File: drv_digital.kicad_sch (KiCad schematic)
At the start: 7 parts, among them U10 74LVC1G19, U11 74HCT595, U12 ULN2803A

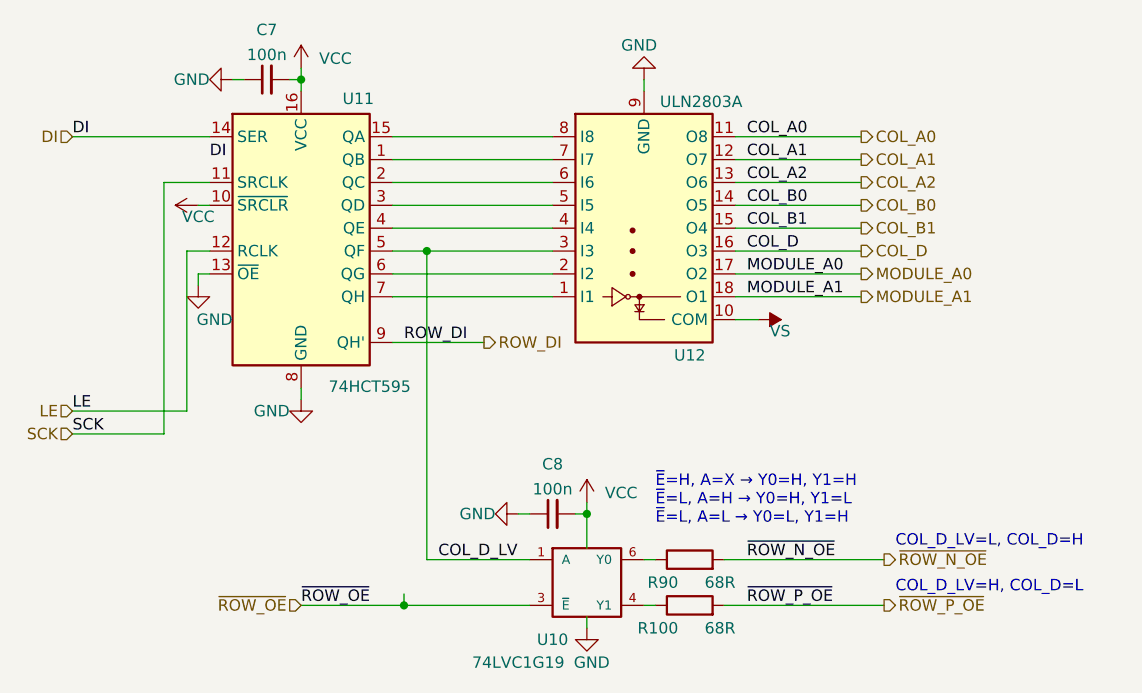
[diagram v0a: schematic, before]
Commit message: Change negative drivers to a TLE75008-ESD, octal low side driver.
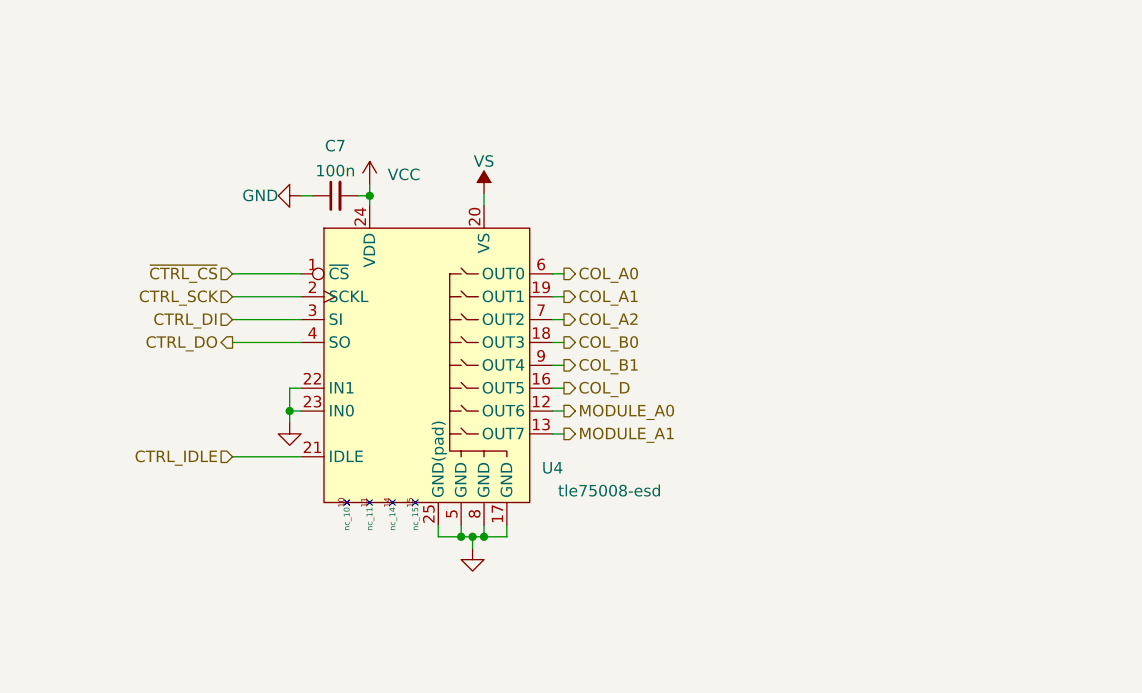
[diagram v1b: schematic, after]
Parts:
- removed C8: 100n, Capacitor_SMD:C_0603_1608Metric, symbol Device:C_Small
- removed R100, R90: 68R, Resistor_SMD:R_0603_1608Metric, symbol Device:R
- removed U10: 74LVC1G19, Package_TO_SOT_SMD:SOT-563, symbol 74xGxx:74LVC1G19
- removed U11: 74HCT595, Package_SO:SOIC-16_3.9x9.9mm_P1.27mm, symbol 74xx:74HCT595
- removed U12: ULN2803A, Package_SO:SOIC-18W_7.5x11.6mm_P1.27mm, symbol Transistor_Array:ULN2803A
- added U4: tle75008-esd, vogelchr_package_so:Infineon-PG-TSDSO-24-51, symbol vogelchr_ic:tle75008-esd
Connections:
- net COL_A0: now also U4.6 (OUT0)
- net COL_A1: now also U4.19 (OUT1)
- net COL_A2: now also U4.7 (OUT2)
- net COL_B0: now also U4.18 (OUT3)
- net COL_B1: now also U4.9 (OUT4)
- net COL_D: now also U4.16 (OUT5)
- net GND: now also U4.17 (GND), U4.22 (IN1), U4.23 (IN0), U4.25 (GND(pad)), U4.5 (GND), U4.8 (GND)
- net MODULE_A0: now also U4.12 (OUT6)
- net MODULE_A1: now also U4.13 (OUT7)
- net VCC: now also U4.24 (VDD)
- net VS: now also U4.20 (VS)
- new net CTRL_DI: U4.3 (SI)
- new net CTRL_DO: U4.4 (SO)
- new net CTRL_IDLE: U4.21 (IDLE)
- new net CTRL_SCK: U4.2 (SCKL)
- new net ~{CTRL_CS}: U4.1 (~{CS})
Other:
- note removed: "COL_D_LV=H, COL_D=L"
- note removed: "COL_D_LV=L, COL_D=H"
- note removed: "~{E}=H, A=X → Y0=H, Y1=H ~{E}=L, A=H → Y0=H, Y1=L ~{E}=L, A=L → Y0=L, Y1=H"
- moved on the sheet: C7
